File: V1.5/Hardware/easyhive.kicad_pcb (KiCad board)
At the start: 2 copper layers, 35 x 75 mm, 104 parts, among them IC1 ATSAMD21G, IC2 BQ2407X, IC3 ADS1232, IC4 DS18B20U, IC5 XC6220B331, IC6 SARA-N310, IC7 TPS22919, J1 U.FL, J2 U.FL(2), K1 693043020611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

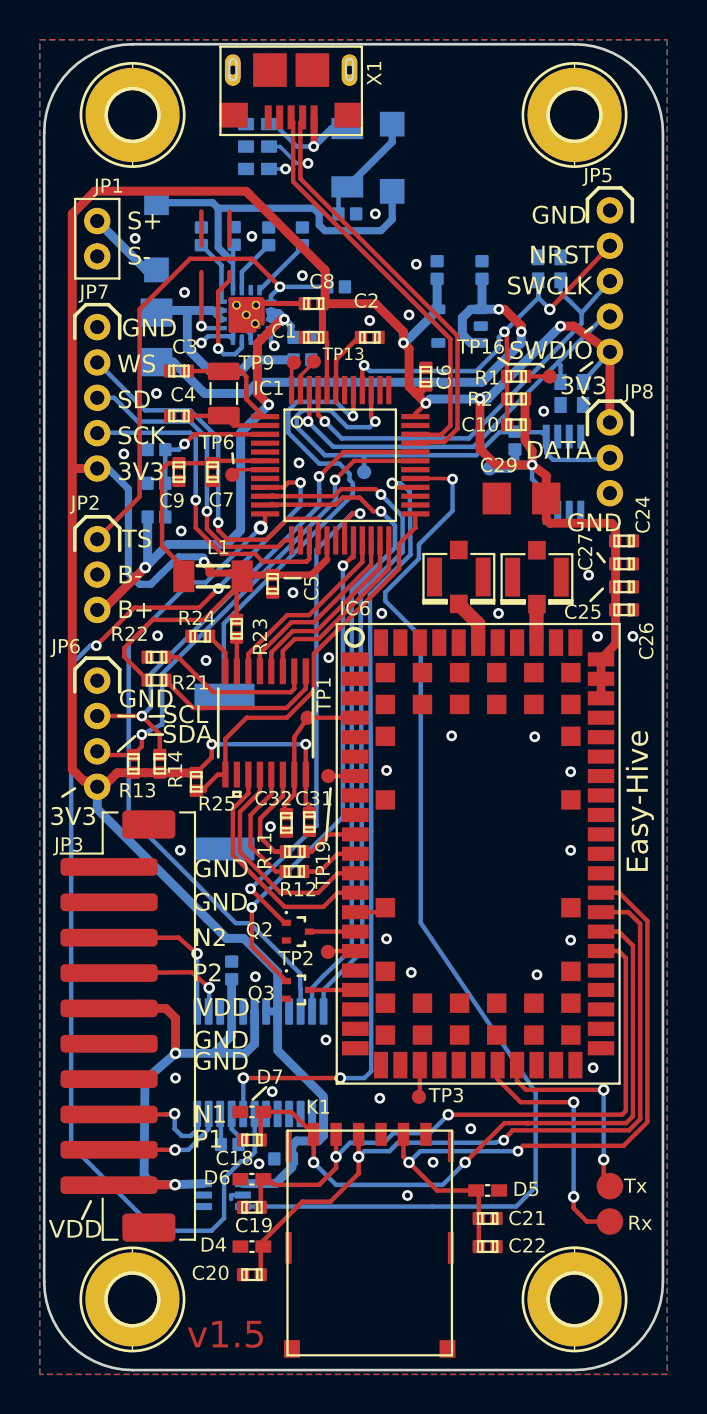
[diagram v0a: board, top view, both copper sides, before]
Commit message: only visualization
remove tracks from LED1 + LED2
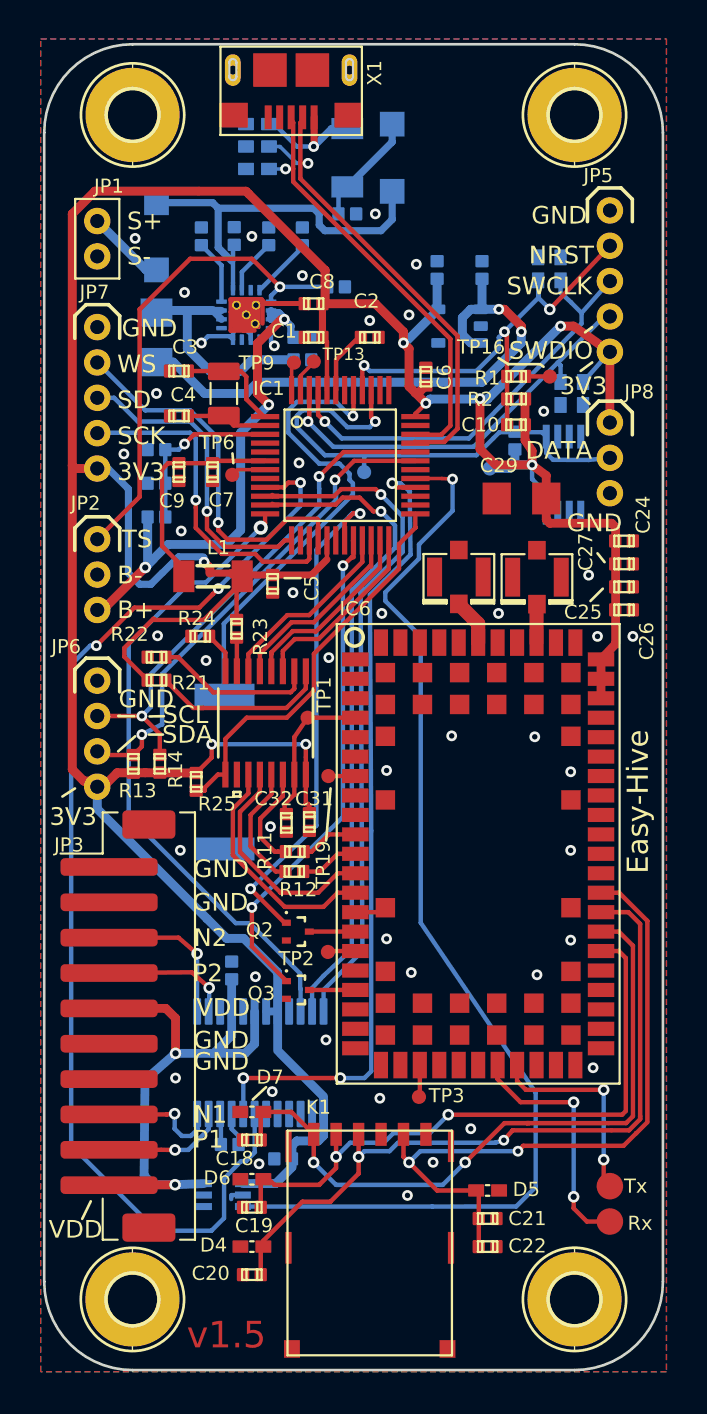
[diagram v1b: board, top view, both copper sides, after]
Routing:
- net Net-(IC2-Pad7): track 6.66 -> 0.00 mm, vias 1 -> 0
- net Net-(IC2-Pad9): track 4.25 -> 0.00 mm, vias 1 -> 0
- net Net-(LED2-PadA): track 1.92 -> 0.00 mm
- net Net-(LED1-PadA): track 1.92 -> 0.00 mm

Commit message: changed Footprints IC2, Q2,Q3,X1 to SMD
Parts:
- L1, L2: value SM-1206 -> (none)

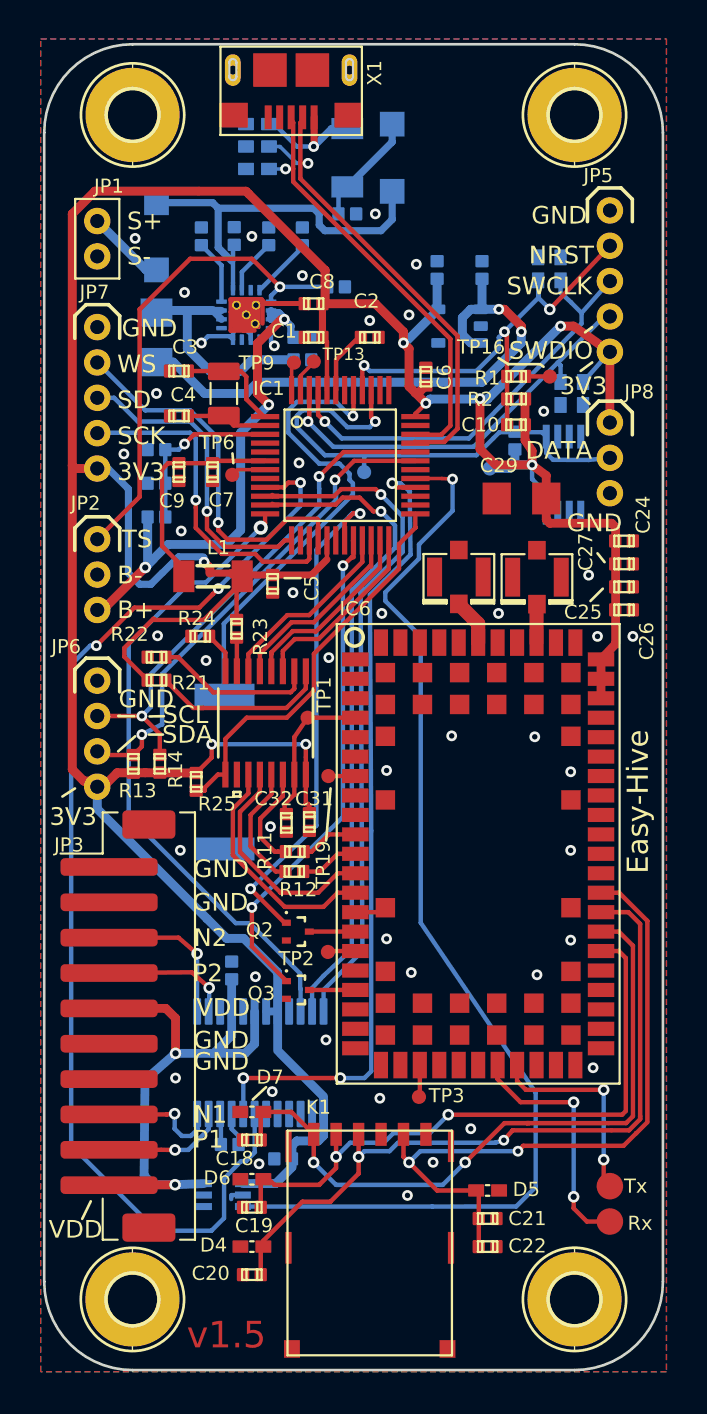
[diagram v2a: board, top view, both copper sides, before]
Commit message: only visualization
-add Point to footprints U1, IC7, P1, D1, D2
-move TP1 (hidden by U1)
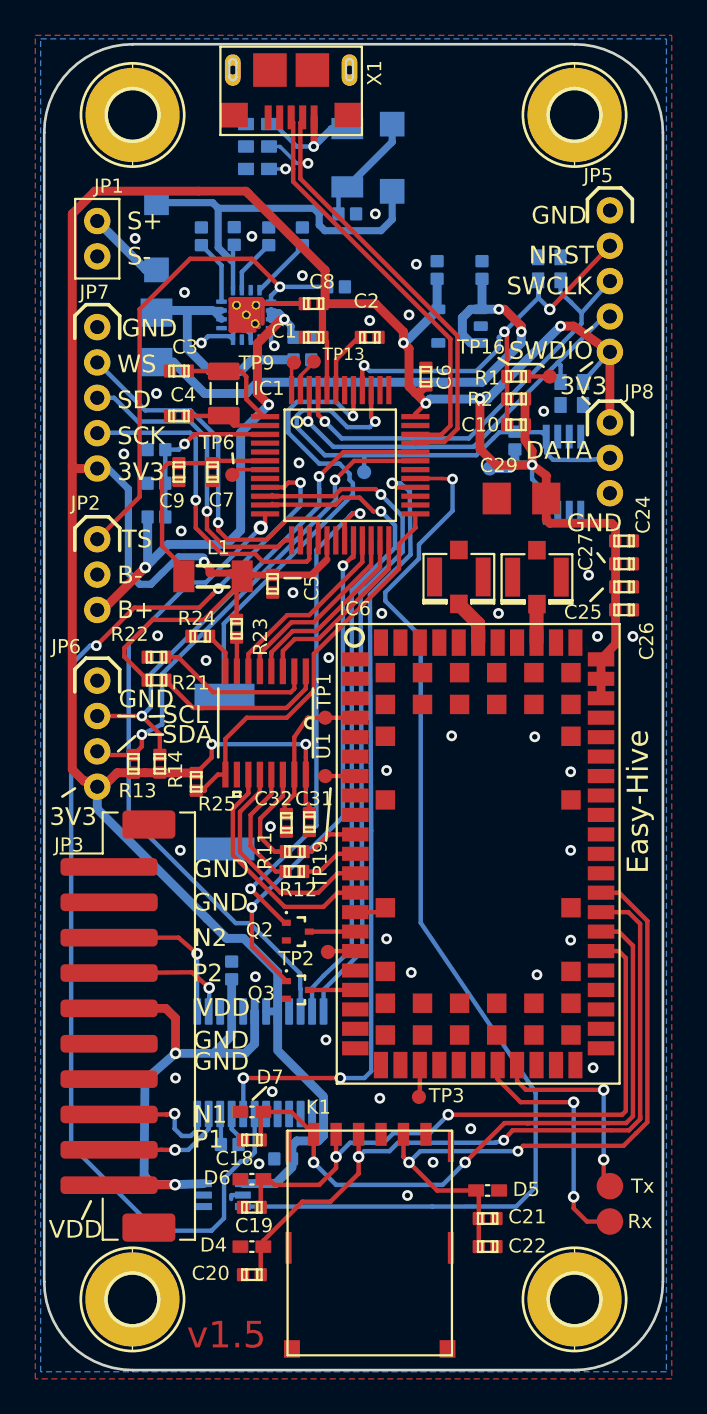
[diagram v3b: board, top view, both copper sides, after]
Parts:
- D1, D2: footprint easyhive:SOD123 -> easyhive:SOD-123
- moved TP1 1.00 mm to (146.9, 105.6)
- moved TP19 0.17 mm to (146.9, 108.9)
